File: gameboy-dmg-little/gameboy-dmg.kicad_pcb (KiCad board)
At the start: 2 copper layers, 82.5 x 87.5 mm, 83 parts, among them J1 Conn_01x02, J3 Conn_01x08, J5 Raspberry_Pi_2_3, J6 Conn_01x09, J7 USB_B_Micro, J8 Conn_01x02, P1 RK10J_POT, SW1 SW_DIP_x01, U1 MCP23017_SO, U2 TP4056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

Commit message: Fixed up little board
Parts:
- removed the G*** at (132.5, 122.9)
- removed the REF** at (83.5, 78.4)
- removed the REF** at (157.5, 78.4)
- added REF**: MountingHole_4.5mm, MountingHole:MountingHole_4.5mm, F.Cu at (157.5, 77.1)
- added REF**: MountingHole_4.5mm, MountingHole:MountingHole_4.5mm, F.Cu at (82.5, 77.1)
- J5, R4, R5: moved to B.Cu
- moved J5 48.2 mm to (93.8, 85.7)
- moved JP6 43.2 mm to (141.4, 93.8), turned to 270 degrees
- moved JP1 40.3 mm to (142.0, 82.2), turned to 90 degrees
- moved JP7 40.3 mm to (138.6, 93.8), turned to 270 degrees
- moved J8 37.5 mm to (85.8, 141.3), turned to 90 degrees
- moved R2 37.0 mm to (142.0, 79.0), turned to 270 degrees
- moved P1 32.5 mm to (128.9, 76.3)
- moved C1 31.1 mm to (139.7, 81.8), turned to 270 degrees
- moved R3 28.4 mm to (137.1, 81.8), turned to 90 degrees
- moved JP5 28.0 mm to (101.6, 100.9), turned to 270 degrees
- moved D4 26.6 mm to (101.1, 147.6)
- moved D3 26.6 mm to (101.1, 149.7)
- moved JP13 25.2 mm to (107.0, 80.5), turned to 0 degrees
- moved JP4 24.9 mm to (104.3, 100.9), turned to 270 degrees
- moved C2 23.9 mm to (137.3, 76.3)
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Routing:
- net +5V: track 132.7 -> 80.9 mm, vias 3 -> 1
- net Net-(D3-Pad2): track 38.2 -> 3.60 mm
- net /TP4056_LIPO_BOOST/BAT-: track 47.4 -> 16.5 mm, vias 1 -> 2
- net Net-(C8-Pad2): track 37.5 -> 6.72 mm
- net Net-(D4-Pad1): track 34.1 -> 5.46 mm, vias 1 -> 0
- net Net-(D3-Pad1): track 33.9 -> 5.56 mm, vias 1 -> 0
- net Net-(C10-Pad1): track 125.3 -> 98.3 mm
- net /TP4056_LIPO_BOOST/5V_BOOST: track 57.6 -> 84.4 mm
- net /TFT_BACKLIGHT: track 10.6 -> 35.8 mm
- net /GPIO_SDA_PI: track 14.7 -> 34.5 mm, vias 0 -> 1
- net Net-(C11-Pad1): track 114.7 -> 95.5 mm
- net Net-(C7-Pad1): track 28.7 -> 12.6 mm, vias 0 -> 1
- net /GPIO_SDA: track 21.8 -> 6.09 mm
- net /GPIO_SCK_PI: track 21.1 -> 34.3 mm
- net /GPIO_SCK: track 19.0 -> 8.27 mm
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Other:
- board size 82.5 x 87.5 mm -> 82.5 x 78.7 mm
- board text added: "Backlight Vcc | GPIO"
- board text added: "GPIO Interrupt Port A Port B"
- board text added: "MOSI"
- board text added: "Raspberry Pi Zero Gameboy DMG by Alex Hoffman"
- board text removed: "Audio Filter"
- board text removed: "Backlight GPIO | Vcc"
- board text removed: "EXTRA BUTTONZ"
- board text removed: "GPIO Interrupt Port B Port A"
- board text removed: "ILI9341 TFT"
- board text removed: "MO SI"
- board text removed: "RPi Zero"
- board text removed: "Raspberry Pi Zero Gameboy DMG Shield by Alex Hoffman"
- board text removed: "TUX"
- board text removed: "Volume"

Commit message: Little board gerbers
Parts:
- moved JP8 9.06 mm to (88.1, 92.9), turned to 0 degrees
- moved SW1 3.12 mm to (82.8, 90.0), turned to 180 degrees
- moved D1 3.11 mm to (88.0, 87.1)
- moved R1 3.05 mm to (86.1, 87.1)
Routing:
- net /TP4056_LIPO_BOOST/5V_BOOST: track 84.4 -> 73.3 mm, vias 1 -> 2
- net +5V: track 80.9 -> 76.3 mm
- net Net-(D1-Pad2): track 10.7 -> 7.19 mm
- net Net-(C11-Pad1): track 95.5 -> 94.7 mm

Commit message: Prototypes 1.0
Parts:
- added G***: LOGO, pad:RetroPie_logo, B.Cu at (127.0, 128.5)
- moved G*** 4.44 mm to (93.8, 127.4)
- moved C3 3.18 mm to (92.0, 147.3)
- moved R8 3.18 mm to (87.4, 150.6)
- moved J8 3.18 mm to (82.6, 141.1)
- moved U3 3.18 mm to (89.1, 147.7)
- moved U4 3.18 mm to (85.4, 147.7)
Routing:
- net /TP4056_LIPO_BOOST/BAT+: track 32.7 -> 36.8 mm
- net Net-(C3-Pad1): track 7.20 -> 10.3 mm
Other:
- outline, holes or cut-outs redrawn
- board text added: "Charge LEDs"
- board text removed: "Charge LEDs Enable"

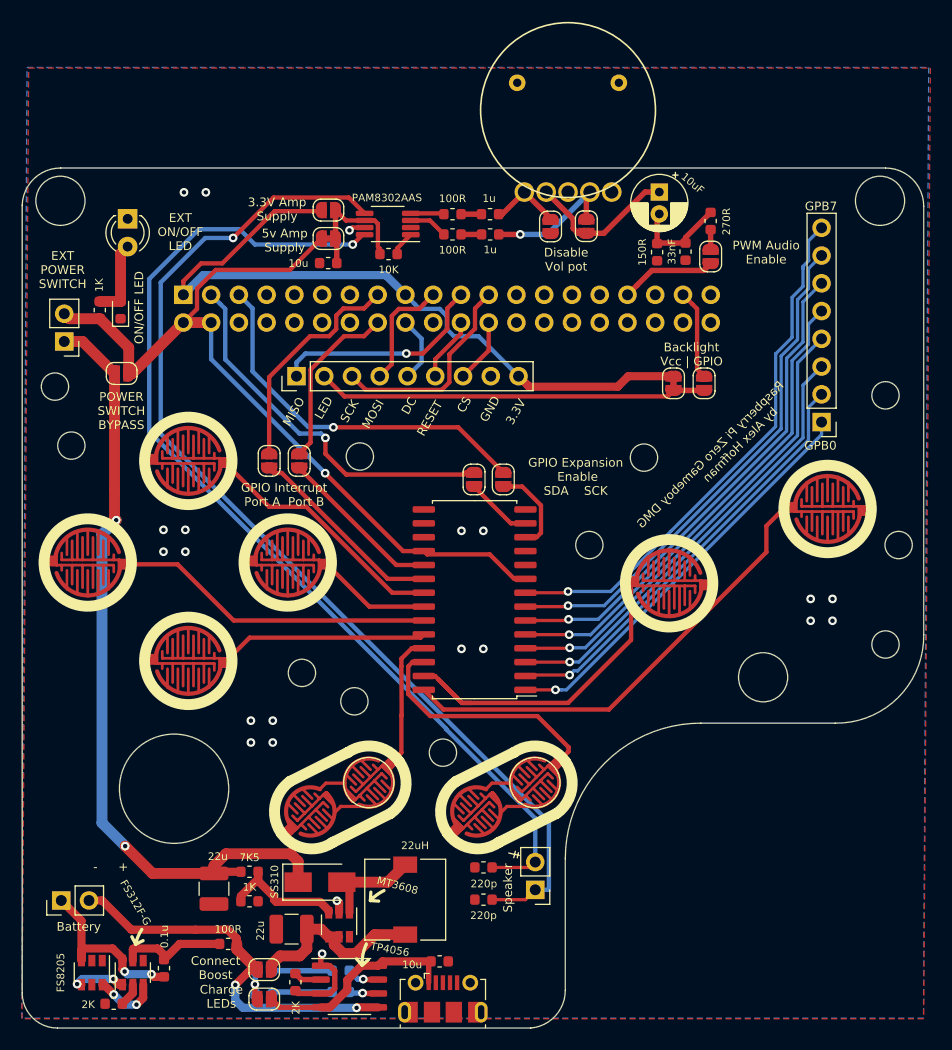
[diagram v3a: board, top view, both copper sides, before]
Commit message: Updated PCBs from initial debugging
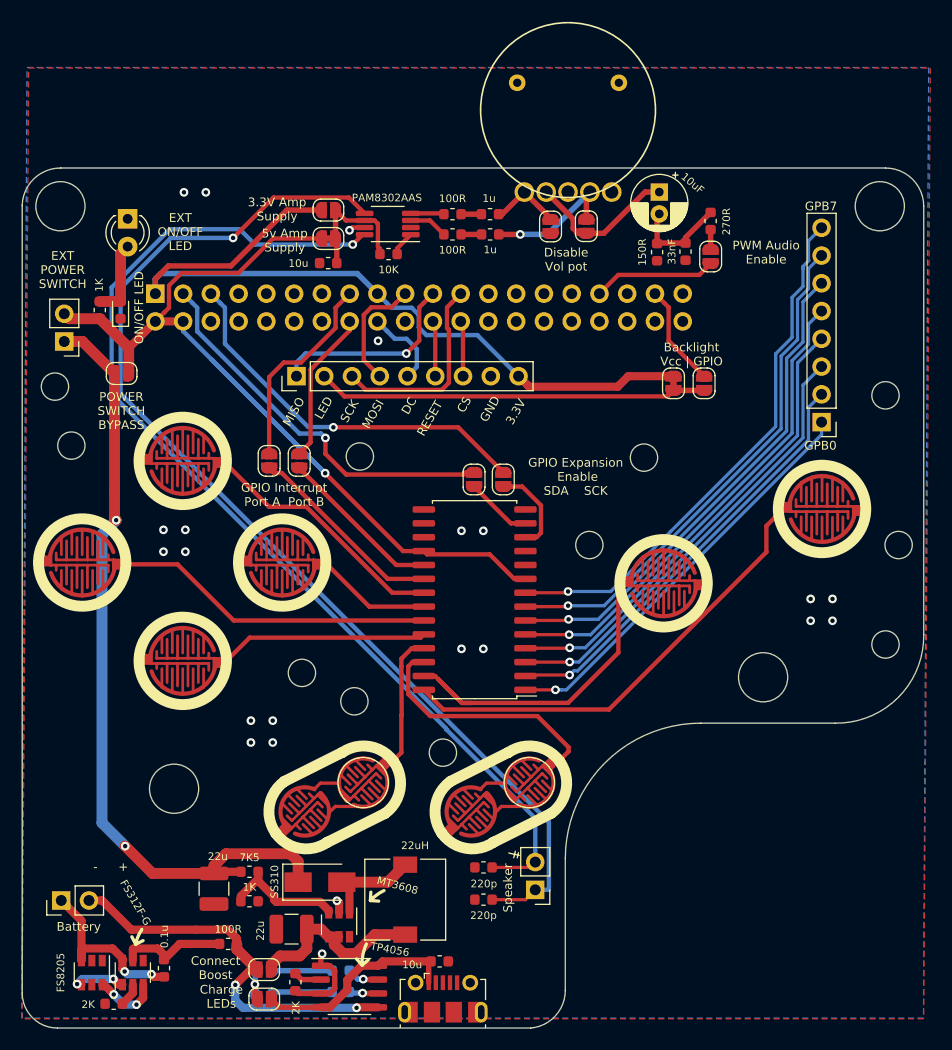
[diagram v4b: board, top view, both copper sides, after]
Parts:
- moved J5 2.57 mm to (91.2, 85.6)
- moved DOWN1 0.51 mm to (93.7, 119.2)
- moved START1 0.51 mm to (120.2, 133.0)
- moved UP1 0.51 mm to (93.7, 100.9)
- moved LEFT1 0.51 mm to (84.5, 110.2)
- moved RIGHT1 0.51 mm to (102.8, 110.2)
- moved SELECT1 0.51 mm to (105.0, 133.0)
- moved A1 0.51 mm to (152.2, 105.3)
- moved B1 0.51 mm to (137.7, 112.1)
- moved REF** 0.50 mm to (157.5, 77.6)
- moved REF** 0.50 mm to (82.5, 77.6)
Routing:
- net +5V: track 76.3 -> 91.4 mm
- net +3V3: track 67.6 -> 73.5 mm
- net Net-(C10-Pad1): track 98.3 -> 103.2 mm
- net Net-(C11-Pad1): track 94.7 -> 99.1 mm
- net Net-(J5-Pad33): track 8.79 -> 11.3 mm
- net /GPIO_INTA_PI: track 20.8 -> 18.6 mm
- net /GPIO_INTB_PI: track 16.1 -> 14.0 mm
- net /TFT_MISO: track 20.0 -> 18.1 mm
- net /TFT_DC: track 6.06 -> 7.49 mm
- net /GPIO_SDA_PI: track 34.5 -> 35.7 mm
- net /TFT_BACKLIGHT_GPIO: track 8.25 -> 9.41 mm
- net /GPIO_SCK_PI: track 34.3 -> 35.5 mm
- net /TFT_SCK: track 19.2 -> 18.4 mm
- net /TFT_RESET: track 5.88 -> 5.10 mm
- net /TFT_CS: track 5.88 -> 5.10 mm
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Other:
- board text added: "V1.1"
